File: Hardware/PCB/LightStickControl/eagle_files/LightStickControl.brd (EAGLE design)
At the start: 23 x 47.4 mm, 24 parts

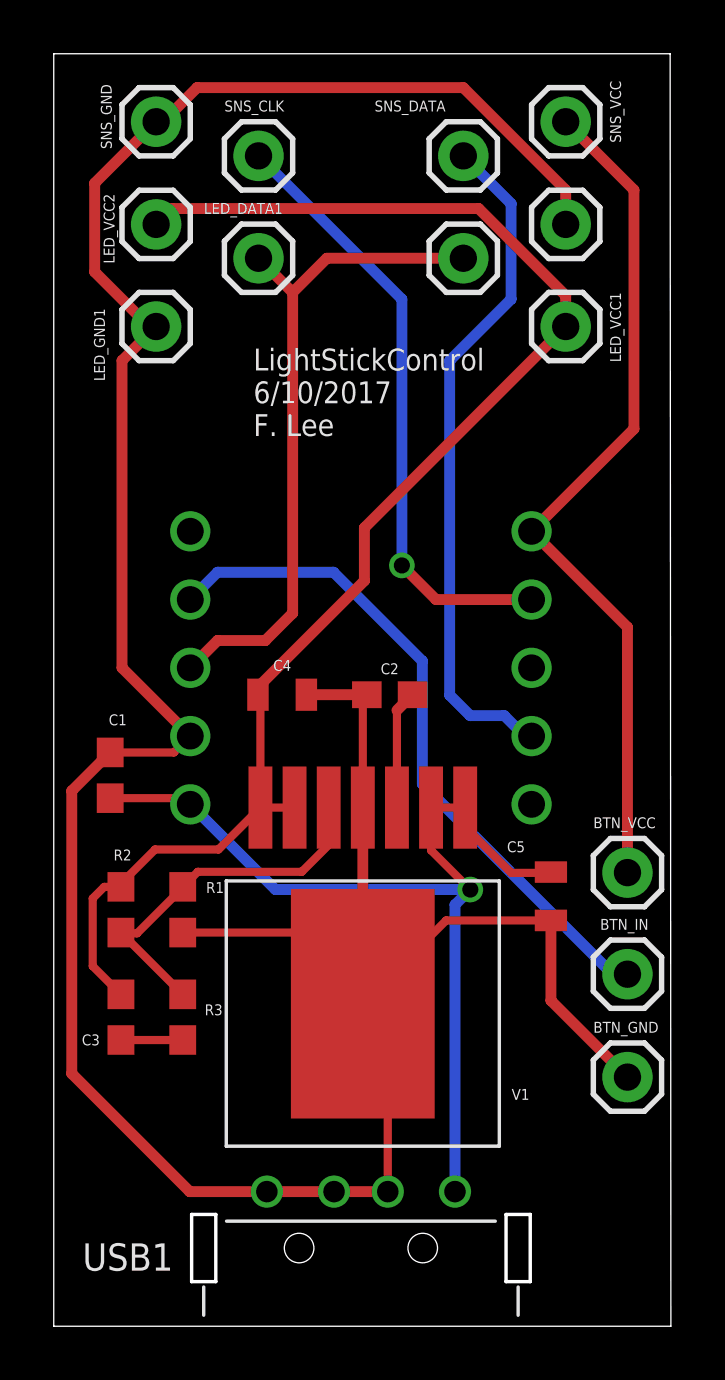
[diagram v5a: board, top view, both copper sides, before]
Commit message: Add ground plane to top layer.
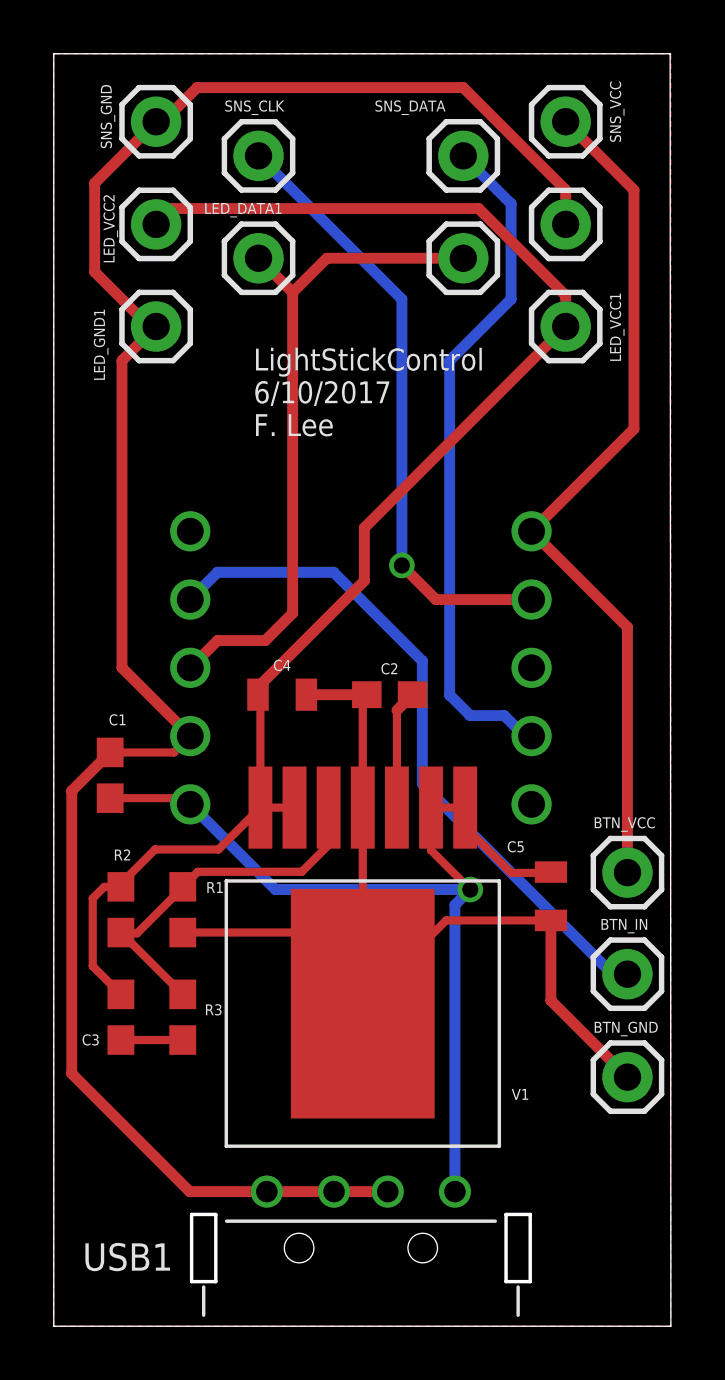
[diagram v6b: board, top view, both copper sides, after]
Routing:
- net GND: track 117.5 -> 112.7 mm
- added copper zone on layer 1, net GND
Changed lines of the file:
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@@
 <contactref element="R1" pad="1"/>
 <wire x1="3.81" y1="37.2" x2="2.54" y2="35.93" width="0.4064" layer="1"/>
-<wire x1="11.5" y1="19.3" x2="11.5" y2="14.45" width="0.4064" layer="1"/>
-<wire x1="11.5" y1="14.45" x2="11.5" y2="12" width="0.4064" layer="1"/>
 <wire x1="11.5" y1="19.3" x2="11.5" y2="23.35" width="0.3048" layer="1"/>
 <wire x1="11.5" y1="23.35" x2="11.65" y2="23.5" width="0.4064" layer="1"/>
@@
 <wire x1="18.5" y1="15.1" x2="18.5" y2="12.118" width="0.4064" layer="1"/>
 <wire x1="18.5" y1="12.118" x2="21.348" y2="9.27" width="0.4064" layer="1"/>
-<wire x1="12.43" y1="5.01" x2="12.43" y2="10.14" width="0.3048" layer="1"/>
-<wire x1="12.43" y1="10.14" x2="11.73" y2="10.84" width="0.3048" layer="1"/>
-<wire x1="11.73" y1="10.84" x2="11.73" y2="11.77" width="0.3048" layer="1"/>
-<wire x1="11.73" y1="11.77" x2="11.5" y2="12" width="0.4064" layer="1"/>
-<wire x1="4.8" y1="14.65" x2="11.3" y2="14.65" width="0.3048" layer="1"/>
-<wire x1="11.3" y1="14.65" x2="11.5" y2="14.45" width="0.4064" layer="1"/>
 <wire x1="9.4" y1="23.5" x2="11.65" y2="23.5" width="0.4064" layer="1"/>
 <wire x1="19.05" y1="41" x2="19.05" y2="42.28" width="0.4064" layer="1"/>
@@
 <wire x1="0.67" y1="9.4" x2="0.67" y2="19.92" width="0.4064" layer="1"/>
 <wire x1="0.67" y1="19.92" x2="2.1" y2="21.35" width="0.4064" layer="1"/>
-<wire x1="3.81" y1="37.2" x2="3.556" y2="37.2" width="0" layer="19" extent="1-1"/>
 <wire x1="10.43" y1="5.01" x2="7.93" y2="5.01" width="0.4064" layer="1"/>
+<polygon width="0.3048" layer="1">
+<vertex x="0" y="47.35"/>
+<vertex x="22.96" y="47.35"/>
+<vertex x="22.96" y="0"/>
+<vertex x="0" y="0"/>
+</polygon>
+<wire x1="4.8" y1="14.65" x2="11.5" y2="14.65" width="0.3048" layer="1"/>
+<wire x1="11.5" y1="14.65" x2="11.5" y2="12" width="0.3048" layer="1"/>
+<wire x1="11.5" y1="19.3" x2="11.5" y2="12" width="0.3048" layer="1"/>
 </signal>
 <signal name="VCC_IN">
